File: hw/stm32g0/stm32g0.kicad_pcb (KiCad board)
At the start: 4 copper layers, 80 x 40 mm, 68 parts, among them J101 Barrel_Jack_Switch, J102 Screw_Terminal_01x03, J201 Conn_01x06, J202 Conn_01x04, J203 Conn_01x03, Q101 BC817, SW401 SW_Push, SW402 SW_Push, SW403 SW_Push, SW404 SW_Push, SW405 SW_Push, SW406 SW_Push, U201 STM32G030K8Tx, U202 74AHCT125, U203 CAT24C256, U301 VS1838B, U401 4050, U501 AMS1117-3.3

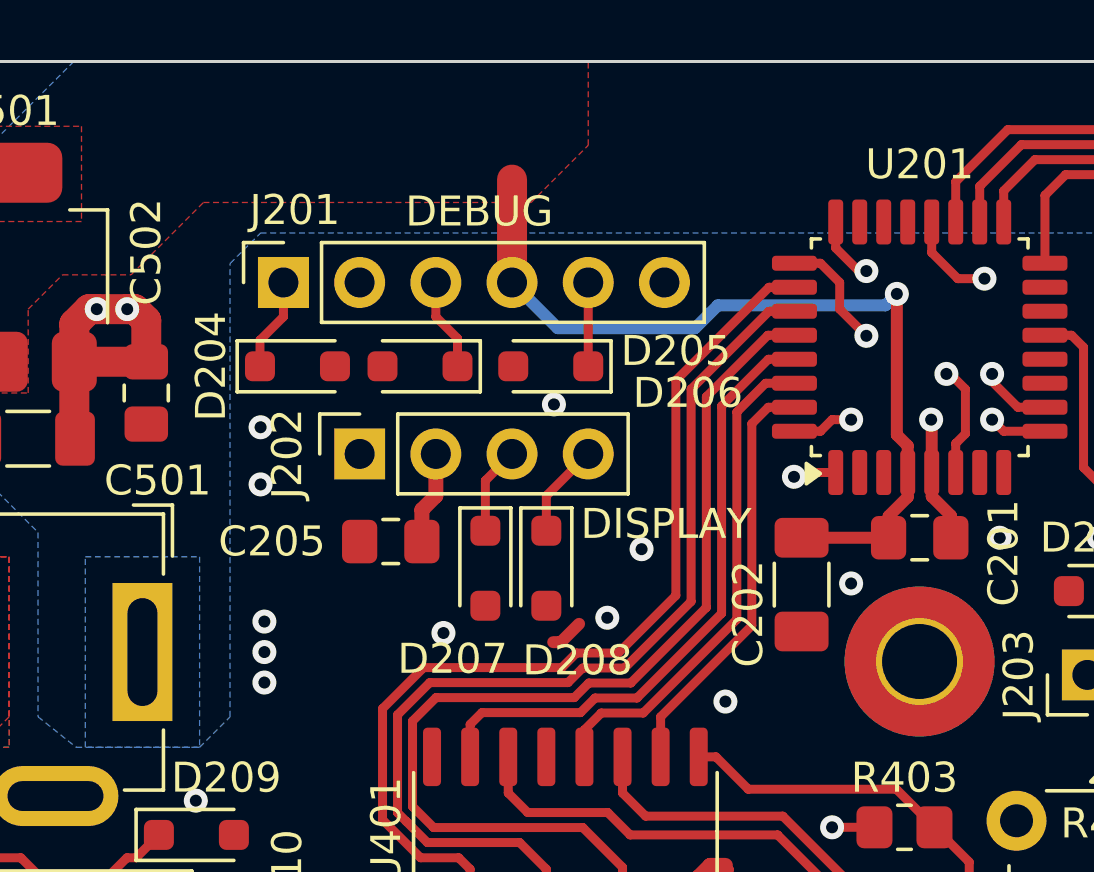
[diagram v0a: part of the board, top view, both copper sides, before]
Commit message: chore(hw): update debug stm32g0 debug port pinout
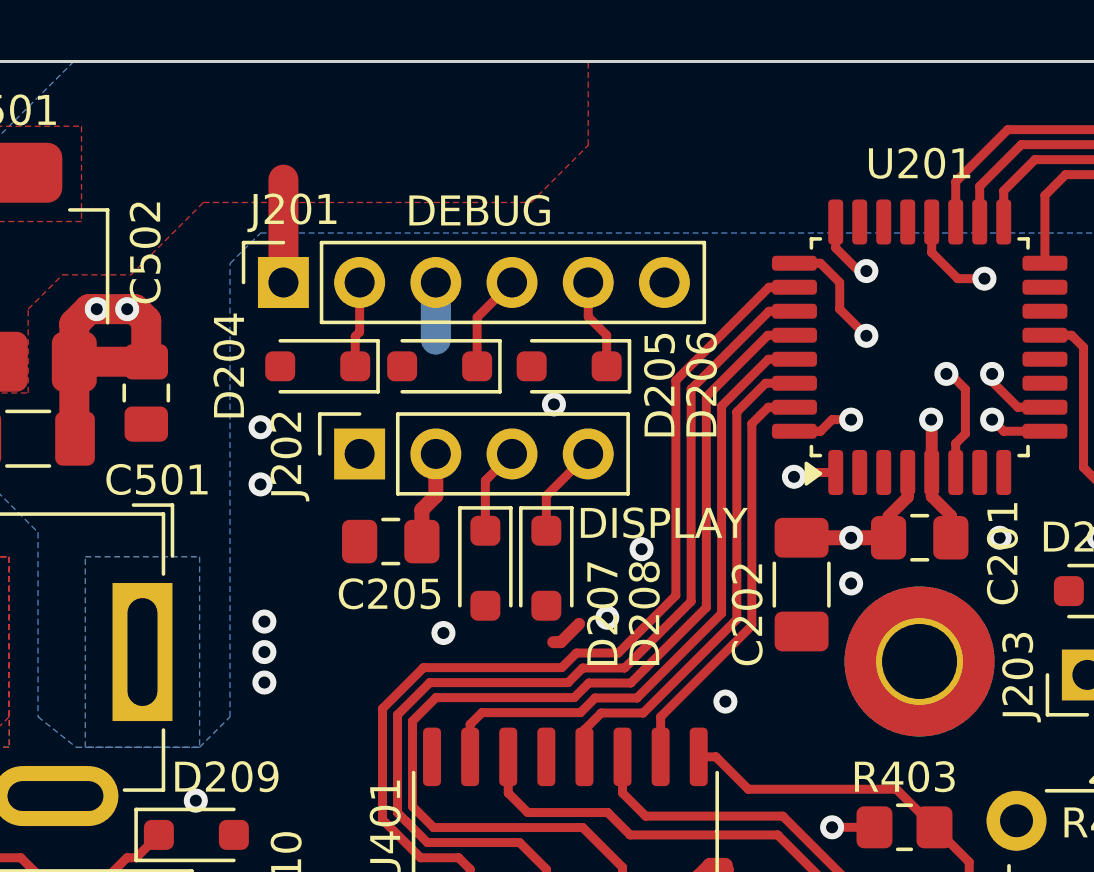
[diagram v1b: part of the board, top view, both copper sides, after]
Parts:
- moved D204 0.67 mm to (139.3, 85.1), turned to 180 degrees
- moved D205 0.66 mm to (143.4, 85.1)
- moved D206 0.61 mm to (147.7, 85.1)
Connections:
- J201 pad 1: /CPU/SWCLK -> +3.3V
- J201 pad 2: GND -> /CPU/SWCLK
- J201 pad 3: /CPU/SWDIO -> GND
- J201 pad 4: +3.3V -> /CPU/SWDIO
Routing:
- net GND: track 278.3 -> 281.7 mm
- net /CPU/SWCLK: track 34.1 -> 31.3 mm
- net +3.3V: track 194.1 -> 191.7 mm
- net /CPU/SWDIO: track 33.8 -> 31.5 mm

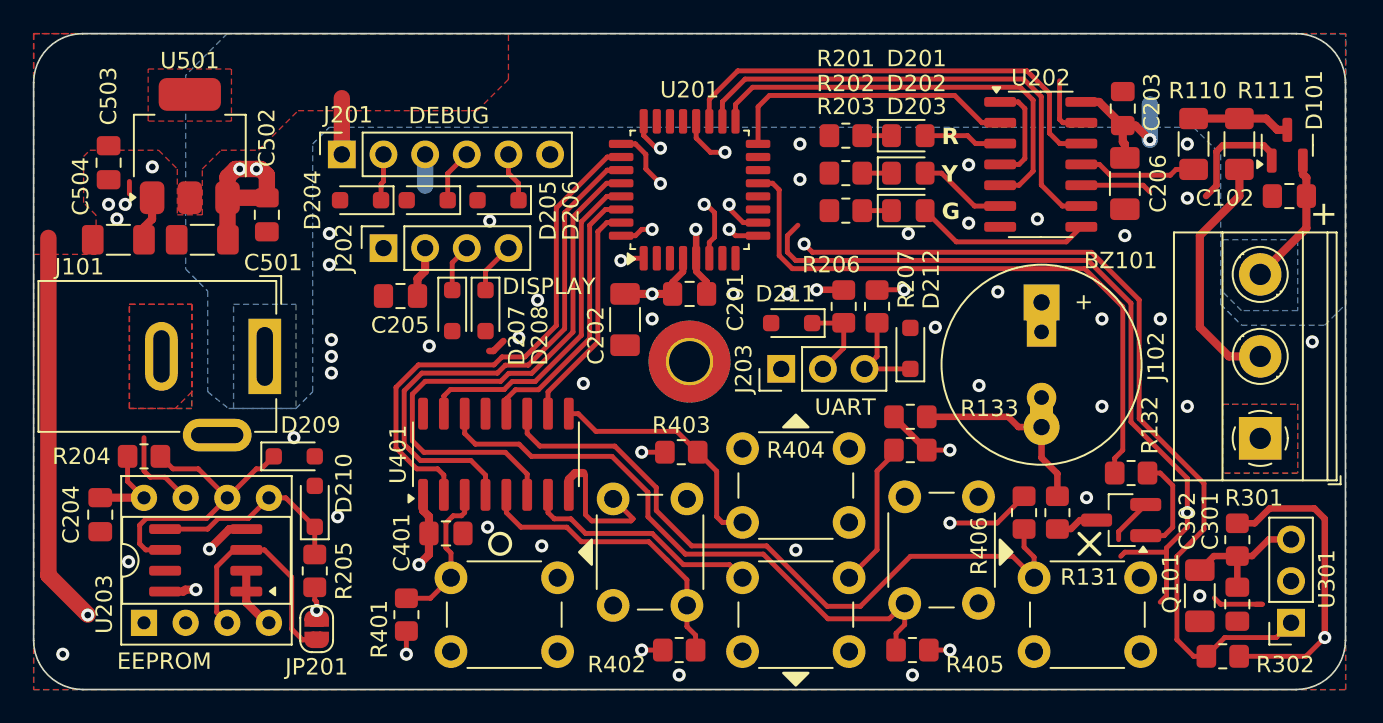
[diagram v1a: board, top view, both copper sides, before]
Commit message: chore(hw): general improvements, utilize some unused CPU pins
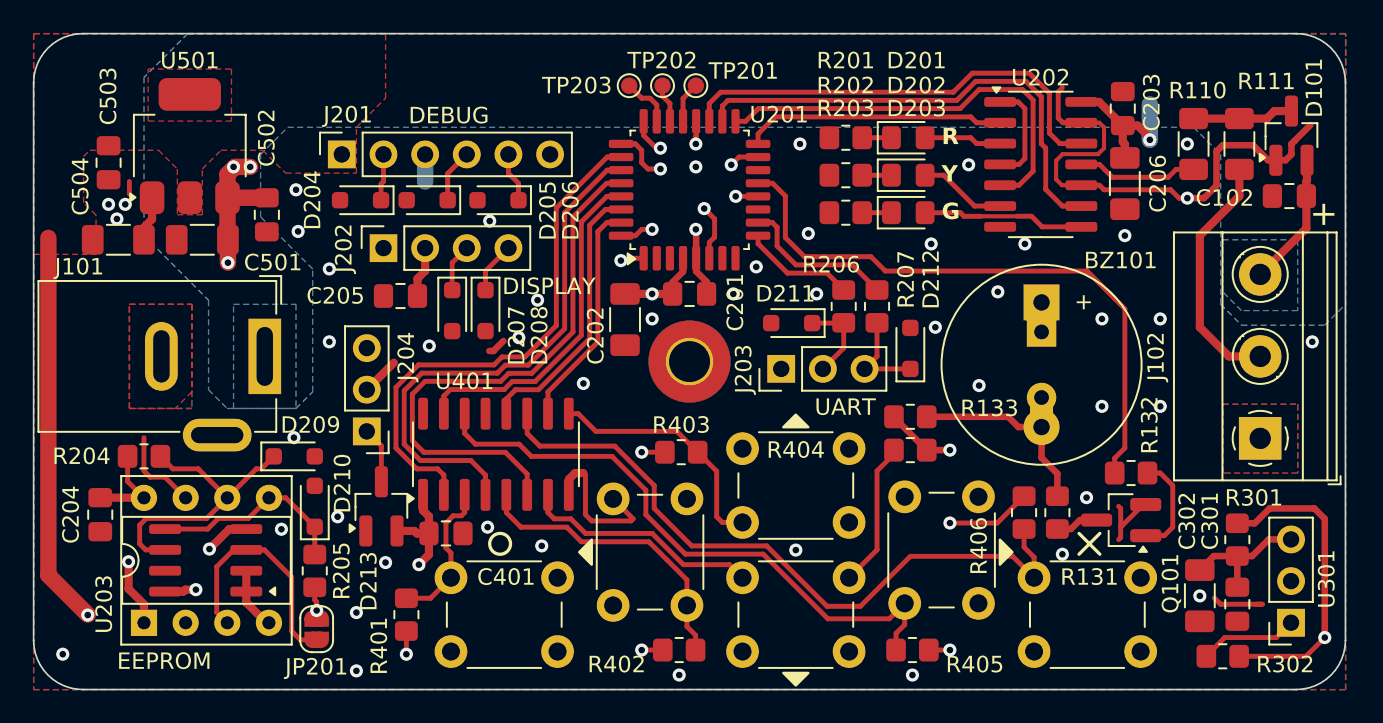
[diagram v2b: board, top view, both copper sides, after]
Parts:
- added D213: BAV199, Package_TO_SOT_SMD:SOT-23_Handsoldering, F.Cu at (140.6, 103.8)
- added J204: Conn_01x03, Connector_PinHeader_2.54mm:PinHeader_1x03_P2.54mm_Vertical, F.Cu at (139.7, 99.2)
- added TP201: TestPoint, TestPoint:TestPoint_Pad_D1.0mm, F.Cu at (159.8, 78.1)
- added TP202: TestPoint, TestPoint:TestPoint_Pad_D1.0mm, F.Cu at (157.7, 78.1)
- added TP203: TestPoint, TestPoint:TestPoint_Pad_D1.0mm, F.Cu at (155.7, 78.1)
- D101: footprint Package_TO_SOT_SMD:SOT-23 -> Package_TO_SOT_SMD:SOT-23_Handsoldering
- moved D101 0.64 mm to (196.1, 81.2)
- moved D202 0.13 mm to (172.7, 83.6)
- moved D203 0.13 mm to (172.7, 85.9)
- moved R202 0.13 mm to (168.9, 83.6)
- moved R203 0.13 mm to (168.9, 85.9)
- moved D201 0.13 mm to (172.7, 81.3)
- moved R201 0.13 mm to (168.9, 81.3)
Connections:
- J201 pad 6: unconnected-(J201-Pin_6-Pad6) -> /CPU/DBG_SPARE
- U201 pad 12: unconnected-(U201-PA5-Pad12) -> /CPU/DBG_SPARE
- U201 pad 15: unconnected-(U201-PB0-Pad15) -> /CPU/MIC_AIN
- U201 pad 21: unconnected-(U201-PA10/NC-Pad21) -> /CPU/DEBUG_1
- U201 pad 22: unconnected-(U201-PA11/PA9-Pad22) -> /CPU/DEBUG_2
- U201 pad 23: unconnected-(U201-PA12/PA10-Pad23) -> /CPU/DEBUG_3
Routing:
- net GND: track 281.7 -> 234.8 mm, vias 48 -> 51
- net /CPU/MIC_AIN: track 0.00 -> 37.9 mm, vias 0 -> 1
- net +3.3V: track 191.7 -> 213.9 mm
- net /CPU/DBG_SPARE: track 0.00 -> 13.7 mm, vias 0 -> 1
- net /CPU/DEBUG_RX: track 16.9 -> 9.64 mm, vias 2 -> 0
- net /CPU/SWCLK: track 31.3 -> 27.6 mm
- net /CPU/SWDIO: track 31.5 -> 27.9 mm
- net /CPU/DEBUG_TX: track 10.4 -> 6.89 mm, vias 2 -> 0
- net /CPU/IR_DATA_3V3: track 63.8 -> 67.4 mm, vias 2 -> 1
- net /CPU/DEBUG_3: track 0.00 -> 3.17 mm
- net /CPU/DEBUG_1: track 0.00 -> 2.50 mm
- net /CPU/DEBUG_2: track 0.00 -> 2.36 mm
- net /CPU/STATUS_LED1: track 18.0 -> 15.9 mm
- net +5V: track 176.1 -> 175.1 mm, vias 9 -> 10
- net Net-(D203-A): track 10.7 -> 9.89 mm
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
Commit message: chore(hw): move all signals to outer layers
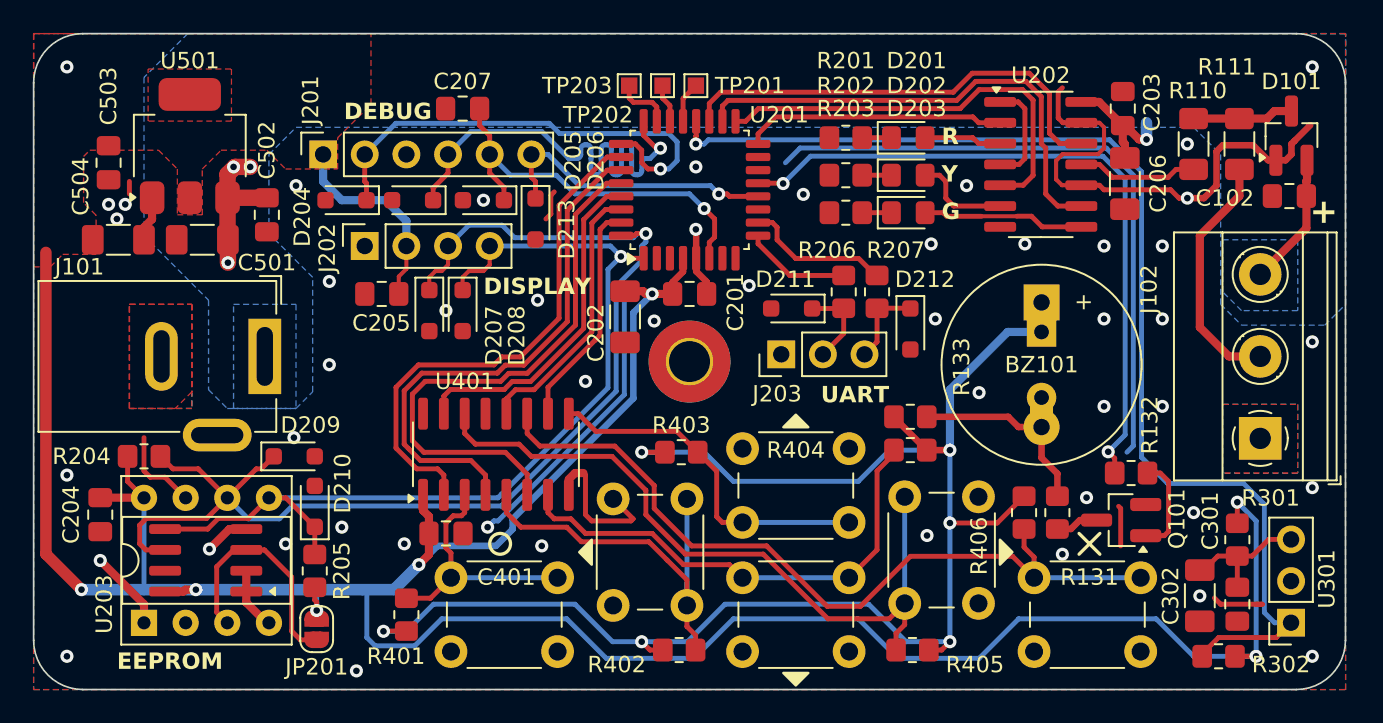
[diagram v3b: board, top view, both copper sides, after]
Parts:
- removed J204: Conn_01x03, Connector_PinHeader_2.54mm:PinHeader_1x03_P2.54mm_Vertical
- added C207: 100n, Capacitor_SMD:C_0805_2012Metric_Pad1.18x1.45mm_HandSolder, F.Cu at (145.5, 79.5)
- D213: value BAV199 -> PESD3V3L1BA; footprint Package_TO_SOT_SMD:SOT-23_Handsoldering -> Diode_SMD:D_SOD-323_HandSoldering
- TP201, TP202, TP203: footprint TestPoint:TestPoint_Pad_D1.0mm -> TestPoint:TestPoint_Pad_1.0x1.0mm
- moved D213 19.9 mm to (150.0, 86.2), turned to -90 degrees
- moved D207 1.40 mm to (143.5, 91.8)
- moved D208 1.40 mm to (145.5, 91.8)
- moved D212 1.18 mm to (172.8, 92.9), turned to -90 degrees
- moved C205 1.15 mm to (140.6, 90.8)
- moved J202 1.15 mm to (139.6, 87.9)
- moved J201 1.14 mm to (137.0, 82.3)
- moved D205 0.89 mm to (142.5, 85.1)
- moved D211 0.89 mm to (165.6, 91.7)
- moved J203 0.89 mm to (165.0, 94.5)
- moved R206 0.89 mm to (168.8, 90.7)
- moved R207 0.89 mm to (170.8, 90.7)
- moved D204 0.89 mm to (138.4, 85.1)
- moved D206 0.89 mm to (146.8, 85.1)
- moved R302 0.25 mm to (191.6, 112.9)
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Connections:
- D213 pad 1: GND -> /CPU/DBG_SPARE
- D213 pad 2: +3.3V -> GND
- U201 pad 15: /CPU/MIC_AIN -> unconnected-(U201-PB0-Pad15)
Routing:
- net GND: track 234.8 -> 136.7 mm, vias 51 -> 49
- net +5V: track 175.1 -> 135.6 mm
- net /CPU/MIC_AIN: track 37.9 -> 0.00 mm, vias 1 -> 0
- net +3.3V: track 213.9 -> 181.1 mm, vias 6 -> 7
- net /CPU/I2C_SDA: track 66.7 -> 58.5 mm
- net /CPU/BUZZER_3V3: track 37.3 -> 42.2 mm, vias 0 -> 2
- net /CPU/~{RESET}: track 19.8 -> 24.1 mm
- net /CPU/DBG_SPARE: track 13.7 -> 17.7 mm
- net /CPU/IR_DATA_3V3: track 67.4 -> 70.4 mm
- net /CPU/SWCLK: track 27.6 -> 29.0 mm
- net /CPU/SWDIO: track 27.9 -> 29.2 mm
- net /CPU/I2C_SCL: track 74.5 -> 73.7 mm
- net Net-(D212-A1): track 5.92 -> 5.16 mm
- net /CPU/DEBUG_RX: track 9.64 -> 9.04 mm
- net Net-(D202-A): track 5.36 -> 5.95 mm

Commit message: chore(hw): improve layout, move NRST cap
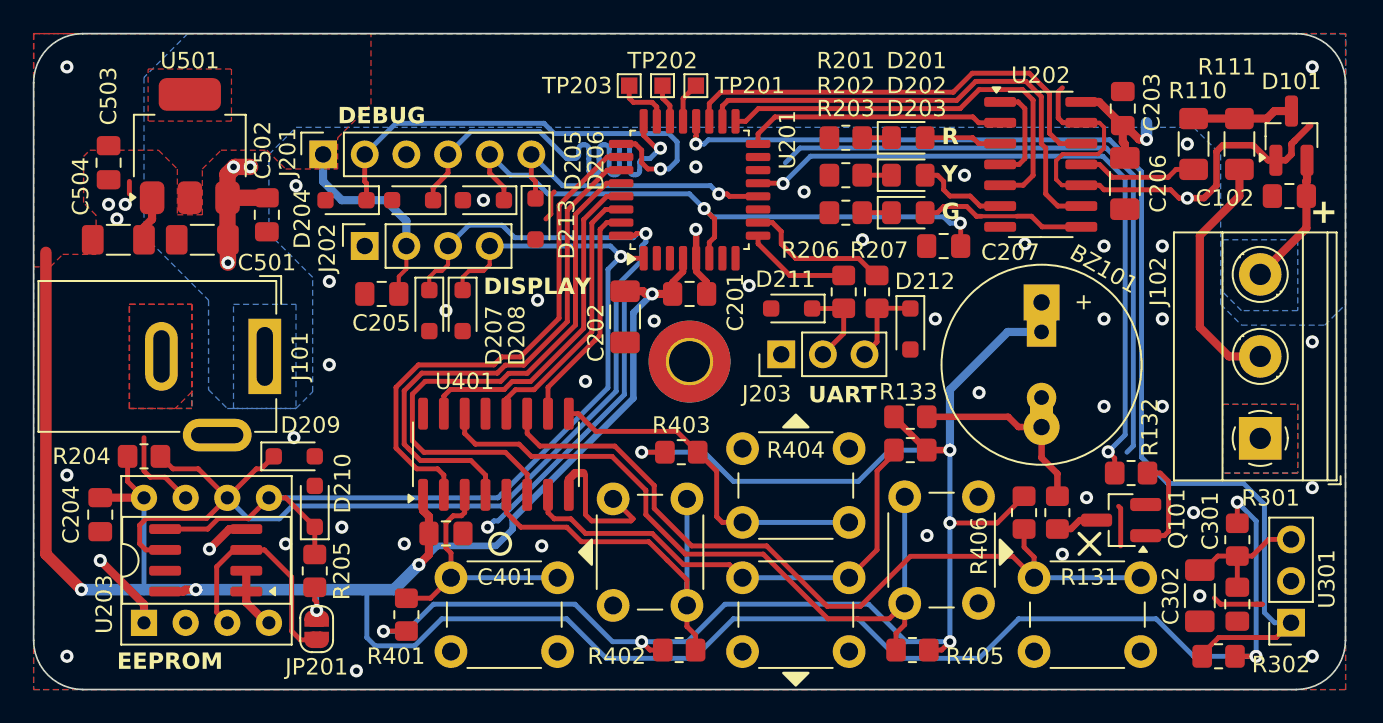
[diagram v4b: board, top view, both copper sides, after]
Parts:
- moved C207 30.5 mm to (174.9, 87.9)
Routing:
- net /CPU/~{RESET}: track 24.1 -> 38.4 mm, vias 1 -> 2

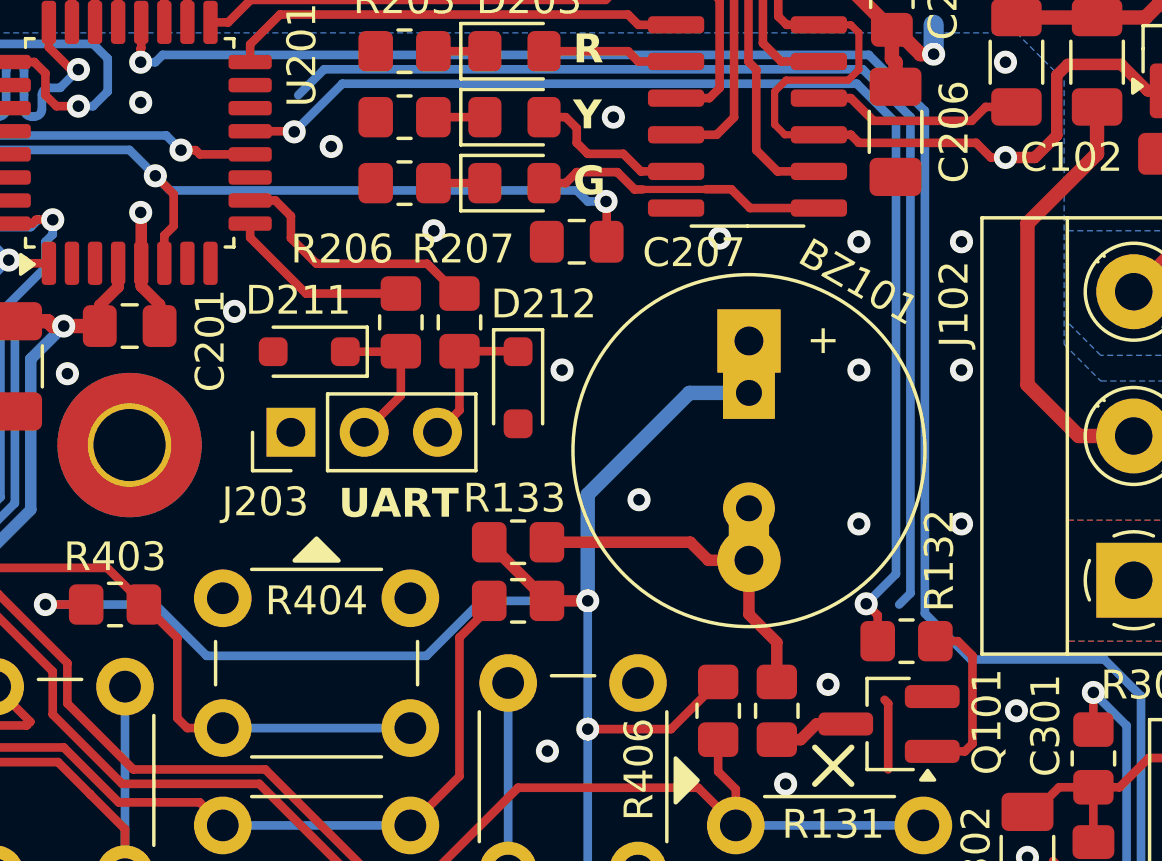
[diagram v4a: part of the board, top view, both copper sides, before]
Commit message: chore(hw): add BT module supply and control pins
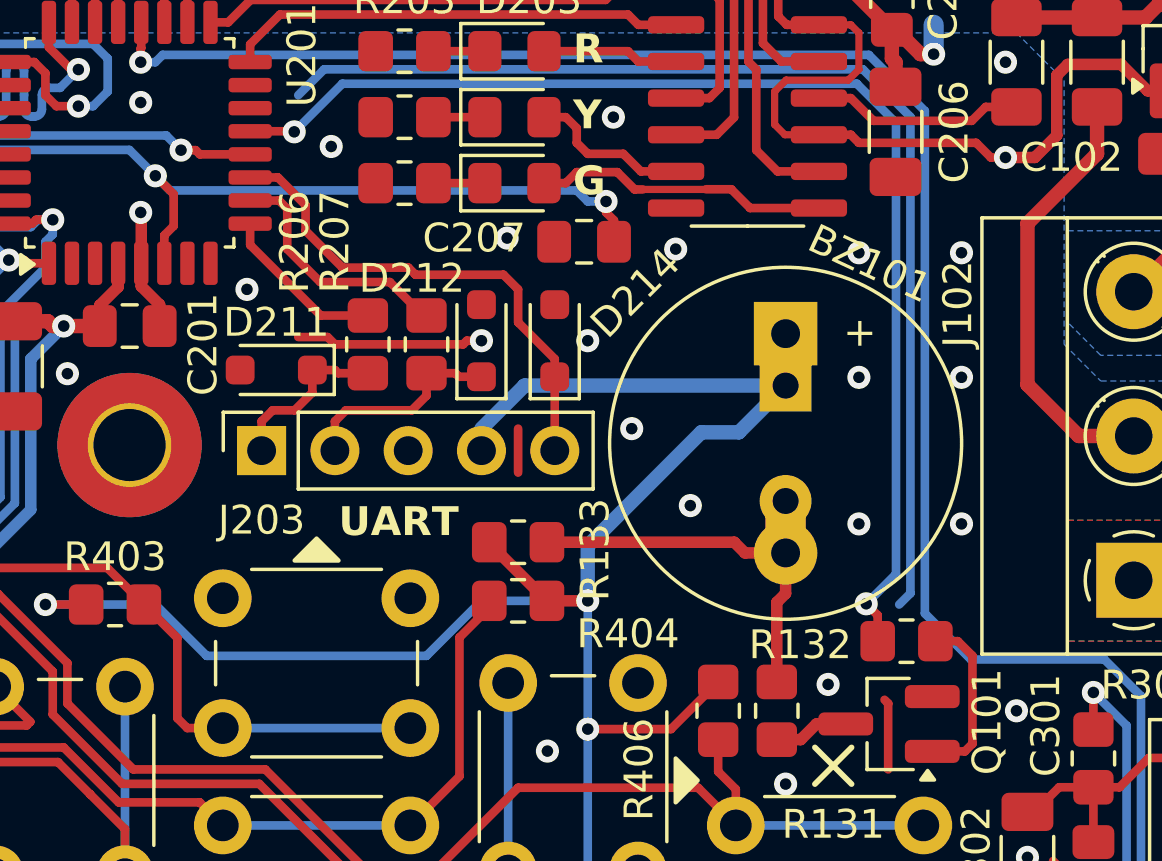
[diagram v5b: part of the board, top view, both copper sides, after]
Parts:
- added D214: PESD3V3L1BA, Diode_SMD:D_SOD-323_HandSoldering, F.Cu at (174.1, 91.3)
- J203: value Conn_01x03 -> Conn_01x05; footprint Connector_PinHeader_2.54mm:PinHeader_1x03_P2.54mm_Vertical -> Connector_PinSocket_2.54mm:PinSocket_1x05_P2.54mm_Vertical
- moved D212 2.07 mm to (171.6, 91.3), turned to 90 degrees
- moved R206 1.37 mm to (167.6, 91.4)
- moved R207 1.37 mm to (169.7, 91.4)
- moved D211 1.31 mm to (164.5, 92.3)
- moved BZ101 1.30 mm to (182.1, 91.1)
- moved J203 1.20 mm to (164.0, 95.1)
- moved C207 0.25 mm to (175.1, 87.9)
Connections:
- net /CPU/DEBUG_RX renamed /CPU/CTRL_RX
- net /CPU/DEBUG_TX renamed /CPU/CTRL_TX
- J203 pad 1: GND -> Net-(D211-A1)
- J203 pad 2: Net-(D211-A1) -> Net-(D212-A1)
- J203 pad 3: Net-(D212-A1) -> GND
- U201 pad 11: unconnected-(U201-PA4-Pad11) -> /CPU/CTRL_EN
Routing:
- net /CPU/CTRL_EN: track 0.00 -> 17.5 mm
- net +5V: track 135.6 -> 145.7 mm
- net GND: track 136.7 -> 144.7 mm, vias 49 -> 51
- net Net-(D212-A1): track 5.16 -> 7.29 mm
- net Net-(BZ101--): track 11.9 -> 13.0 mm
- net /CPU/CTRL_TX: track 6.51 -> 5.83 mm
- net Net-(D211-A1): track 5.27 -> 5.94 mm
